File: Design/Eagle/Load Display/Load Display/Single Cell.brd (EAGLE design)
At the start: 68.2 x 83.8 mm, 12 parts

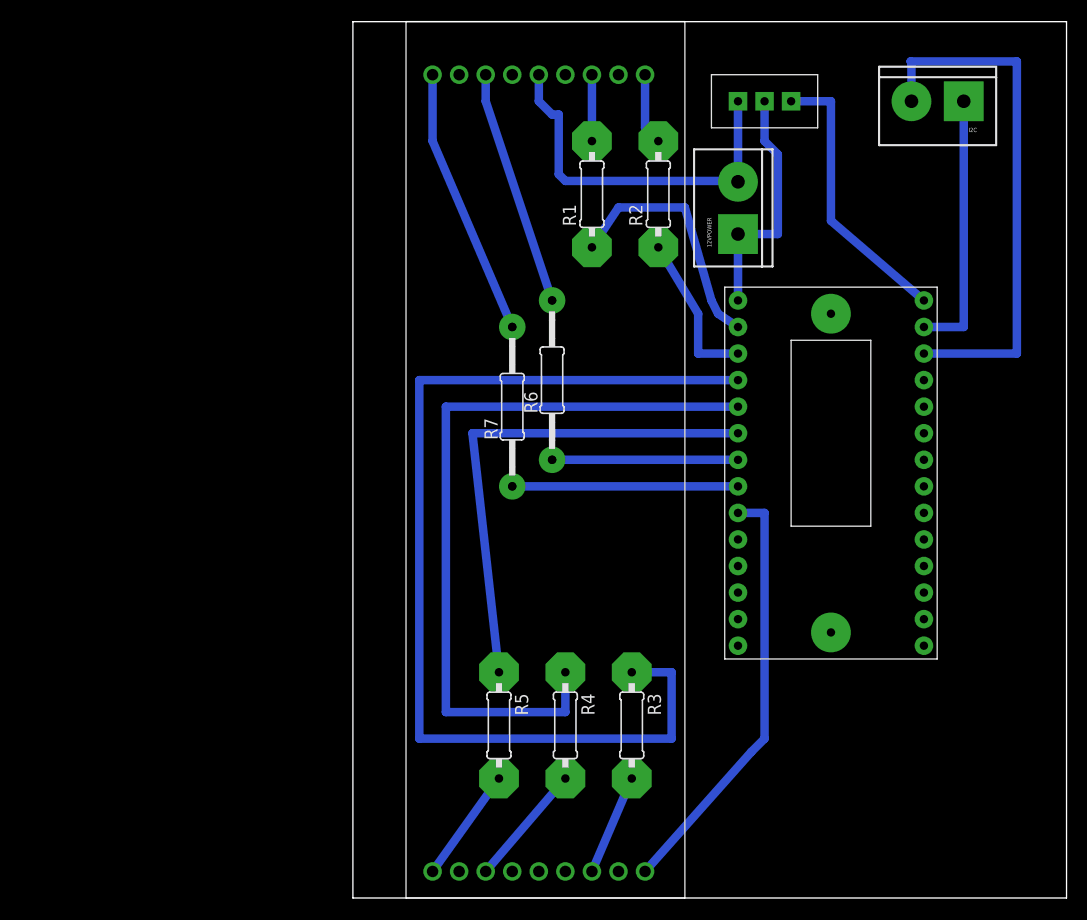
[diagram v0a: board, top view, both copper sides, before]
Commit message: Added a bunch of stuff to make the new 7 segment boards.
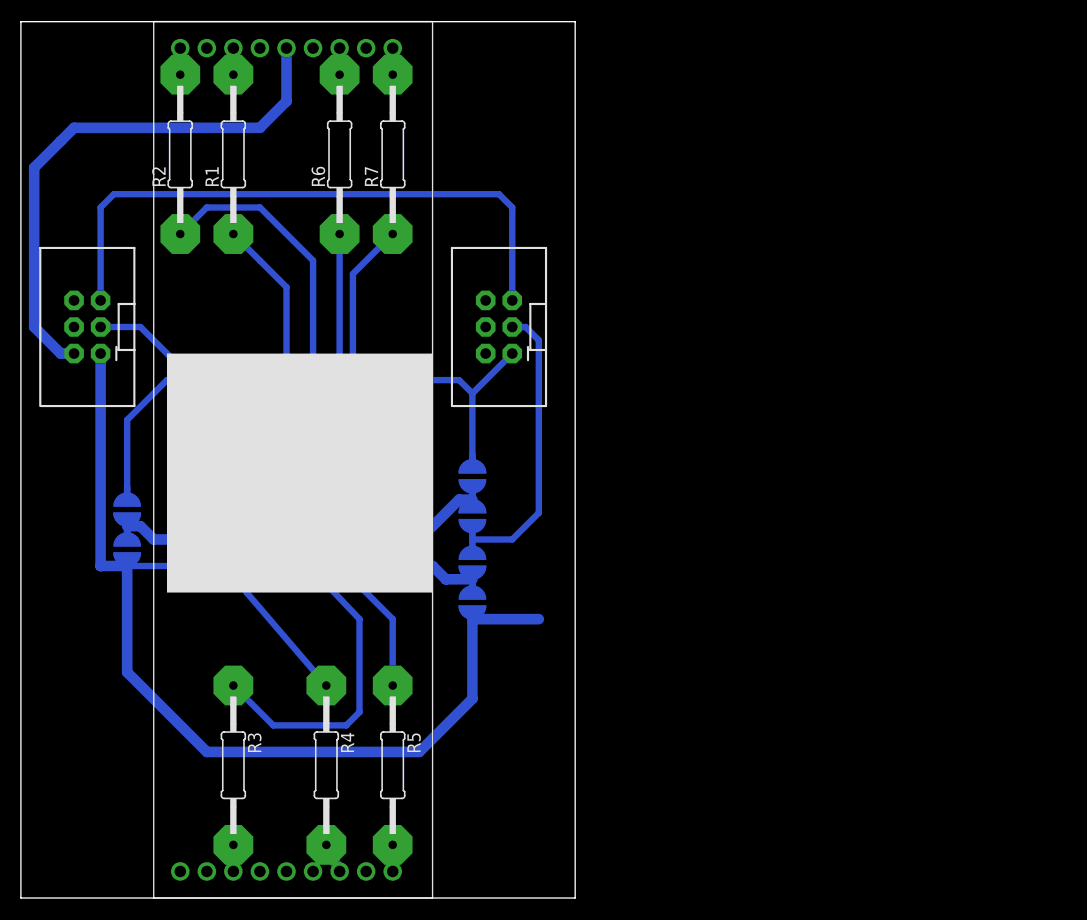
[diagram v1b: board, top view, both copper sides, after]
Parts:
- removed 12VPOWER, I2C: M025MM, Ben-SF-Con:SCREWTERMINAL-5MM-2
- added JP1, JP2: (no value), Ben-SF-Con:2X3-SHROUDED
- added U$2: (no value), Parts:DRIVER_BOARD_ADAFRUIT
- added U$4, U$5, U$6, U$7: SOLDER_JUMPER, Parts:SOLDER_JUMPER
- added U$8: (no value), Parts:DRIVER_BOARD
- DIS1: device Parts:4INTESTER -> Parts:7SEGMENT_BACKWARDS
- R1, R2, R3, R4, R5: device Ben-rcl:0207/10 -> Ben-rcl:0207/15
- U$1: value 5VREG -> SOLDER_JUMPER; device Parts:LM78XX -> Parts:SOLDER_JUMPER
- U$3: value HT16K33BRD -> SOLDER_JUMPER; device Parts:HT16K33BRKOUT -> Parts:SOLDER_JUMPER
- moved U$1 54.5 mm to (43.2, 26.7), flipped to the bottom, turned to 180 degrees
- moved R2 45.9 mm to (15.2, 69.9)
- moved R3 38.3 mm to (20.3, 11.4)
- moved R1 34.5 mm to (20.3, 69.9)
- moved R6 29.6 mm to (30.5, 69.9)
- moved R7 26.7 mm to (35.6, 69.9)
- moved U$3 26.5 mm to (43.2, 30.5), flipped to the bottom, turned to 180 degrees
- moved DIS1 24.1 mm to (15.2, 1.27)
- moved R4 23.2 mm to (29.2, 11.4)
- moved R5 10.9 mm to (35.6, 11.4)
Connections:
- removed net N$18: DIS1.5, U$3.C7
- removed net N$19: U$1.P$3, U$3.VDD
- removed net N$20: 12VPOWER.2, DIS1.8, U$1.P$1
- new net GND: JP1.1, JP2.1, U$1.P$1, U$2.G, U$2.GND, U$4.P$1, U$6.P$1, U$8.G, U$8.GND
- new net N$29: U$1.P$2, U$2.A0, U$3.P$1, U$8.A0
- new net SDA: JP1.6, JP2.6, U$2.SDA, U$8.SDA
- new net SSCL: JP1.5, JP2.5, U$2.SCL, U$8.SCL
- new net VCC12: DIS1.8, JP1.2, JP2.2
- new net VCC5: JP1.3, JP2.3, U$2.VCC, U$3.P$2, U$5.P$2, U$7.P$2, U$8.VCC
- net N$10: now also U$2.DRAIN2, U$8.DRAIN2; no longer U$3.C2
- net N$11: now also U$2.DRAIN3, U$8.DRAIN3; no longer U$3.C3
- net N$12: now also U$2.DRAIN4, U$8.DRAIN4; no longer U$3.C4
- net N$13: now also U$2.DRAIN5, U$8.DRAIN5; no longer U$3.C5
- net N$14: now also U$2.DRAIN6, U$8.DRAIN6; no longer U$3.C6
- net N$15: now also U$2.A1, U$4.P$2, U$5.P$1, U$8.A1; no longer I2C.1, U$3.SDA
- net N$16: now also U$2.A2, U$6.P$2, U$7.P$1, U$8.A2; no longer I2C.2, U$3.SCL
- net N$17: now also U$2.DRAIN7, U$8.DRAIN7; no longer 12VPOWER.1, U$1.P$2, U$3.GND
- net N$8: now also U$2.DRAIN0, U$8.DRAIN0; no longer U$3.C0
- net N$9: now also U$2.DRAIN1, U$8.DRAIN1; no longer U$3.C1
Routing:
- net GND: track 0.00 -> 115.3 mm
- net SSCL: track 0.00 -> 60.7 mm
- net VCC5: track 0.00 -> 55.4 mm
- net N$10: track 99.1 -> 44.4 mm
- net VCC12: track 0.00 -> 51.9 mm
- net N$11: track 72.4 -> 23.7 mm
- net N$16: track 50.8 -> 9.42 mm
- net N$18: track 41.2 -> 0.00 mm
- net N$20: track 35.8 -> 0.00 mm
- net N$9: track 15.0 -> 44.1 mm
- net N$19: track 26.9 -> 0.00 mm
- net N$12: track 48.4 -> 25.0 mm
- net N$7: track 25.7 -> 2.54 mm
- net N$17: track 23.4 -> 2.54 mm
- net N$6: track 22.6 -> 2.54 mm
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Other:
- board size 68.2 x 83.8 mm -> 53 x 83.8 mm

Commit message: Finished the board for the 7 segments.
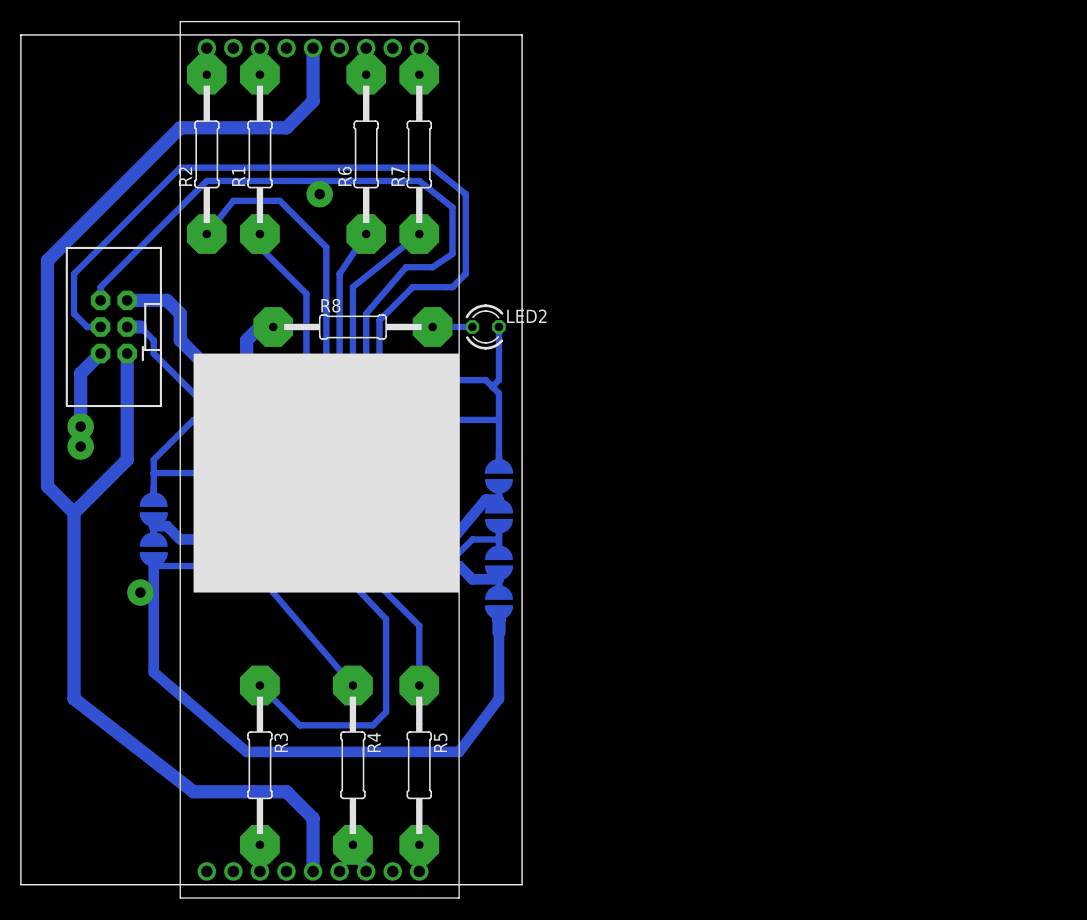
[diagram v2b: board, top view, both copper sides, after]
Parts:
- removed JP1: (no value), Ben-SF-Con:2X3-SHROUDED
- added LED2: TLLR4400, led:LED3MM
- added R8: 1000, Ben-rcl:0207/15
- moved R2 2.54 mm to (17.8, 69.9)
- moved DIS1 2.54 mm to (17.8, 1.27)
- moved R1 2.54 mm to (22.9, 69.9)
- moved R3 2.54 mm to (22.9, 11.4)
- moved R5 2.54 mm to (38.1, 11.4)
- moved R6 2.54 mm to (33.0, 69.9)
- moved U$1 2.54 mm to (45.7, 26.7)
- moved U$2 2.54 mm to (29.2, 39.4)
- moved U$3 2.54 mm to (45.7, 30.5)
- moved U$4 2.54 mm to (45.7, 39.4)
- moved U$5 2.54 mm to (45.7, 35.6)
- moved U$6 2.54 mm to (12.7, 31.8)
- moved U$7 2.54 mm to (12.7, 35.6)
- moved U$8 2.54 mm to (29.2, 39.4)
- moved JP2 2.54 mm to (8.89, 53.3)
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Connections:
- new net N$18: LED2.A, R8.2
- net GND: now also JP2.2, JP2.6, LED2.K; no longer JP1.1, JP2.1
- net SDA: now also JP2.3; no longer JP1.6, JP2.6
- net SSCL: now also JP2.4; no longer JP1.5, JP2.5
- net VCC12: now also DIS1.3, JP2.1; no longer JP1.2, JP2.2
- net VCC5: now also JP2.5, R8.1; no longer JP1.3, JP2.3
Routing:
- net VCC12: track 51.9 -> 129.1 mm
- net GND: track 115.3 -> 172.5 mm
- net VCC5: track 55.4 -> 93.9 mm
- net SSCL: track 60.7 -> 79.7 mm
- net SDA: track 2.54 -> 15.3 mm
- net N$18: track 0.00 -> 3.81 mm
- net N$14: track 27.5 -> 30.8 mm
- net N$8: track 29.3 -> 27.3 mm
- net N$13: track 29.7 -> 31.6 mm
- net N$12: track 25.0 -> 25.9 mm
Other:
- board size 53 x 83.8 mm -> 47.9 x 81.3 mm
